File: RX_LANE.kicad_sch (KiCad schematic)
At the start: 1 part, among them U7 AD8285WBCPZ

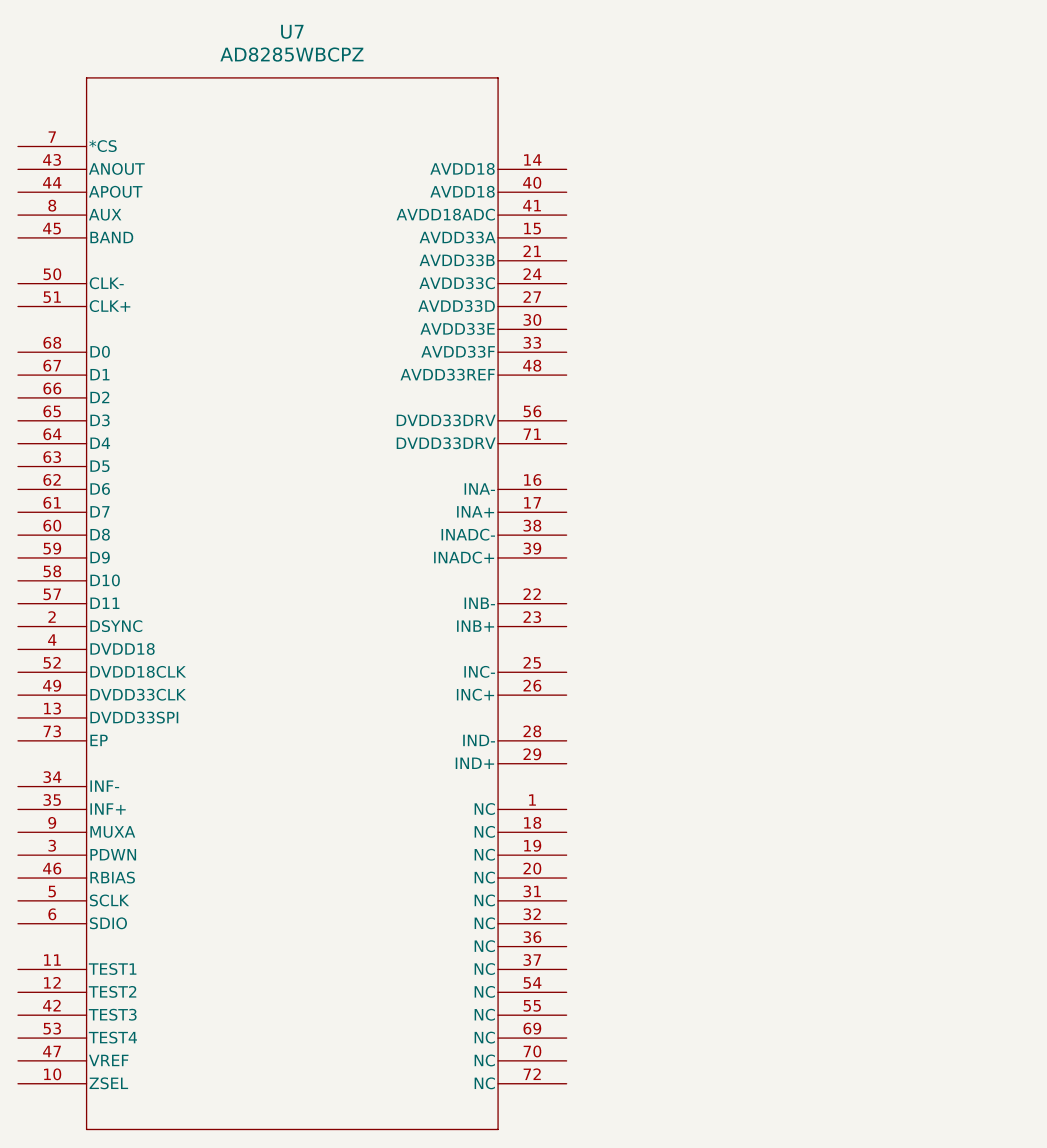
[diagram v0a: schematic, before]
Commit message: added ADC clock fanout, added 3A buck
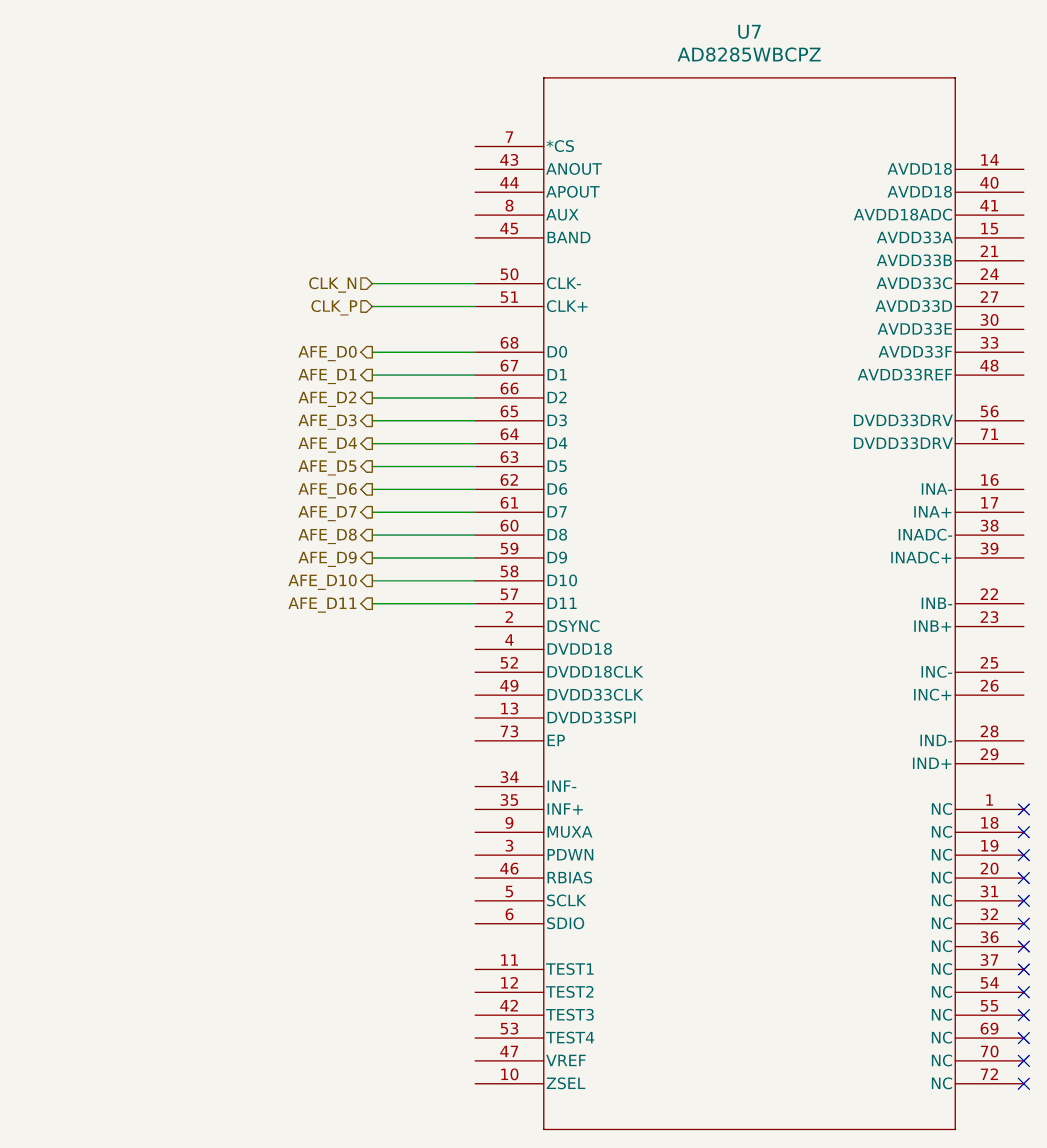
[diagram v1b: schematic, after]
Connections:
- net CLK_N: now reaches U7.50 (CLK-)
- net CLK_P: now reaches U7.51 (CLK+)
- net AFE_D11: now reaches U7.57 (D11)
- net AFE_D10: now reaches U7.58 (D10)
- net AFE_D9: now reaches U7.59 (D9)
- net AFE_D8: now reaches U7.60 (D8)
- net AFE_D7: now reaches U7.61 (D7)
- net AFE_D6: now reaches U7.62 (D6)
- net AFE_D5: now reaches U7.63 (D5)
- net AFE_D4: now reaches U7.64 (D4)
- net AFE_D3: now reaches U7.65 (D3)
- net AFE_D2: now reaches U7.66 (D2)
- net AFE_D1: now reaches U7.67 (D1)
- net AFE_D0: now reaches U7.68 (D0)
- no-connect marks 0 -> 13
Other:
- moved on the sheet: U7

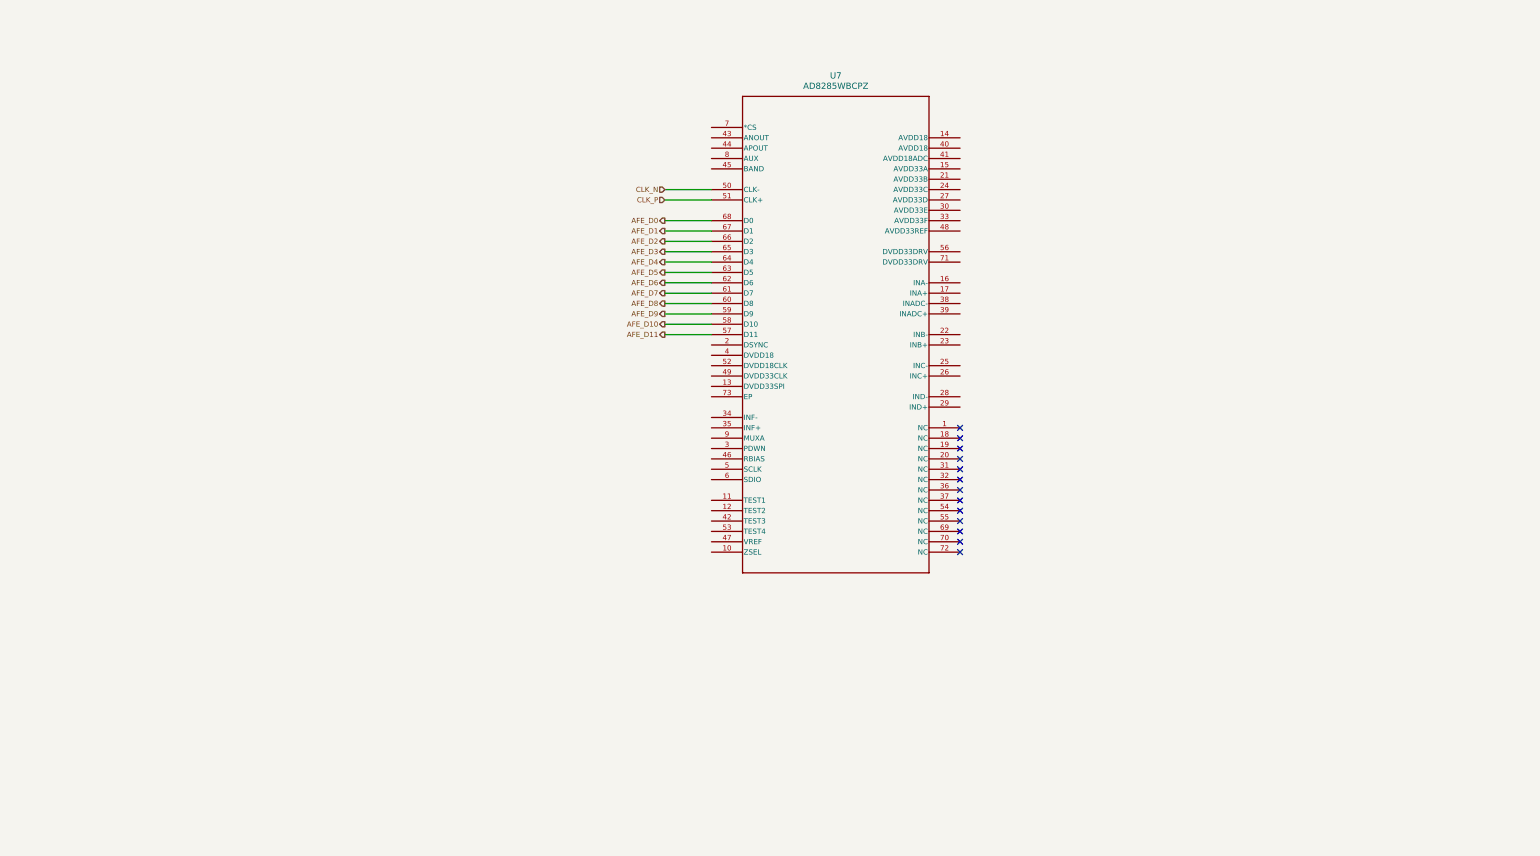
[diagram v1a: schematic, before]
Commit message: finished HV rails (revise, ai), added LDO instances, ready to bind & supply
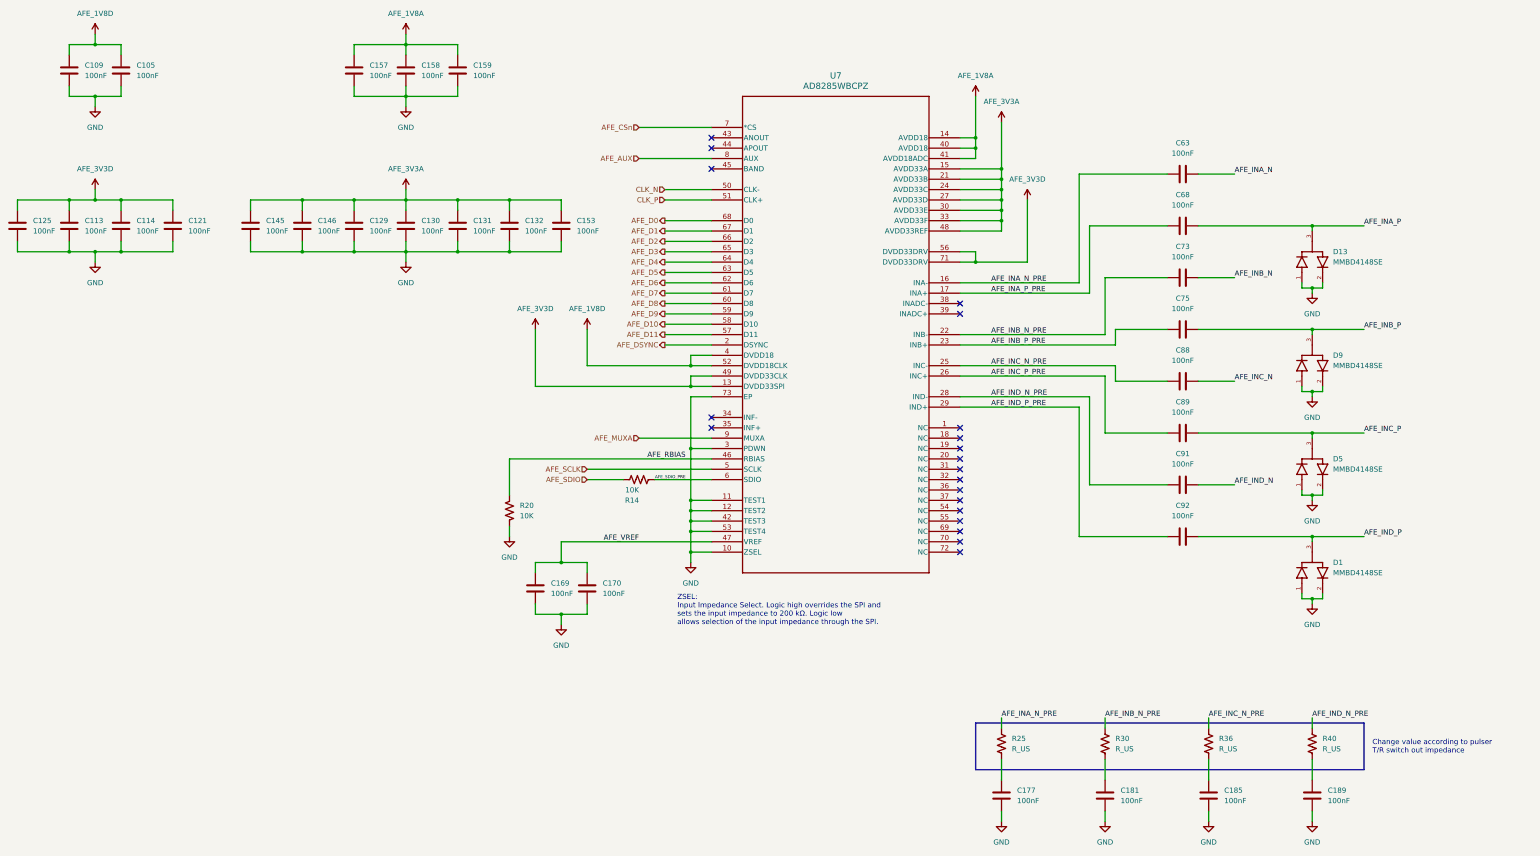
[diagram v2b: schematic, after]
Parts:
- added C105, C109, C113, C114, C121, C125, C129, C130, C131, C132, C145, C146, C153, C157, C158, C159, C169, C170, C177, C181, C185, C189, C63, C68, C73, C75, C88, C89, C91, C92: 100nF, symbol Device:C
- added D1, D13, D5, D9: MMBD4148SE, MMBD4148SE:SOT95P237X112-3N, symbol MMBD4148SE:MMBD4148SE
- added R14, R20: 10K, symbol Device:R_US
- added R25, R30, R36, R40: R_US, symbol Device:R_US
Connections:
- net GND: now reaches U7.10 (ZSEL)
- net GND: now also U7.11 (TEST1), U7.12 (TEST2), U7.3 (PDWN), U7.42 (TEST3), U7.53 (TEST4), U7.73 (EP), C105.2, C109.2, C113.2, C114.2, C121.2, C125.2, C129.2, C130.2, C131.2, C132.2, C145.2, C146.2, C153.2, C157.2, C158.2, C159.2, C169.2, C170.2, C177.2, C181.2, C185.2, C189.2, D1.1, D1.2, D13.1, D13.2, D5.1, D5.2, D9.1, D9.2, R20.2
- net AFE_3V3D: now reaches U7.13 (DVDD33SPI)
- net AFE_3V3D: now also U7.49 (DVDD33CLK), U7.56 (DVDD33DRV), U7.71 (DVDD33DRV), C113.1, C114.1, C121.1, C125.1
- net AFE_1V8A: now reaches U7.14 (AVDD18)
- net AFE_1V8A: now also U7.40 (AVDD18), U7.41 (AVDD18ADC), C157.1, C158.1, C159.1
- net AFE_3V3A: now reaches U7.15 (AVDD33A)
- net AFE_3V3A: now also U7.21 (AVDD33B), U7.24 (AVDD33C), U7.27 (AVDD33D), U7.30 (AVDD33E), U7.33 (AVDD33F), U7.48 (AVDD33REF), C129.1, C130.1, C131.1, C132.1, C145.1, C146.1, C153.1
- net AFE_INA_N_PRE: now reaches U7.16 (INA-)
- net AFE_INA_N_PRE: now also C63.2, R25.1
- net AFE_INA_P_PRE: now reaches U7.17 (INA+)
- net AFE_INA_P_PRE: now also C68.2
- net AFE_DSYNC: now reaches U7.2 (DSYNC)
- net AFE_INB_N_PRE: now reaches U7.22 (INB-)
- net AFE_INB_N_PRE: now also C73.2, R30.1
- net AFE_INB_P_PRE: now reaches U7.23 (INB+)
- net AFE_INB_P_PRE: now also C75.2
- net AFE_INC_N_PRE: now reaches U7.25 (INC-)
- net AFE_INC_N_PRE: now also C88.2, R36.1
- net AFE_INC_P_PRE: now reaches U7.26 (INC+)
- net AFE_INC_P_PRE: now also C89.2
- net AFE_IND_N_PRE: now reaches U7.28 (IND-)
- net AFE_IND_N_PRE: now also C91.2, R40.1
- net AFE_IND_P_PRE: now reaches U7.29 (IND+)
- net AFE_IND_P_PRE: now also C92.2
- net AFE_1V8D: now reaches U7.4 (DVDD18)
- net AFE_1V8D: now also U7.52 (DVDD18CLK), C105.1, C109.1
- net AFE_RBIAS: now reaches U7.46 (RBIAS)
- net AFE_RBIAS: now also R20.1
- net AFE_VREF: now reaches U7.47 (VREF)
- net AFE_VREF: now also C169.1, C170.1
- net AFE_SCLK: now reaches U7.5 (SCLK)
- net AFE_SDIO_PRE: now reaches U7.6 (SDIO)
- net AFE_SDIO_PRE: now also R14.2
- net AFE_CSn: now reaches U7.7 (*CS)
- net AFE_AUX: now reaches U7.8 (AUX)
- net AFE_MUXA: now reaches U7.9 (MUXA)
- new net: C177.1, R25.2
- new net: C189.1, R40.2
- new net: C181.1, R30.2
- new net: C185.1, R36.2
- new net AFE_INA_N: C63.1
- new net AFE_INA_P: C68.1, D13.3
- new net AFE_INB_N: C73.1
- new net AFE_INB_P: C75.1, D9.3
- new net AFE_INC_N: C88.1
- new net AFE_INC_P: C89.1, D5.3
- new net AFE_IND_N: C91.1
- new net AFE_IND_P: C92.1, D1.3
- new net AFE_SDIO: R14.1
- no-connect marks 13 -> 20
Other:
- note added: "Change value according to pulser T/R switch out impedance"
- note added: "ZSEL: Input Impedance Select. Logic high overrides the SPI and sets the input impedance to 200 kΩ. Logic low allows selection of the input impedance through the SPI."

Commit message: almost finished, phew! just dd +/- 5v rails, connect the SDIO & power enable pins and figure out the rest of the clocking chain
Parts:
- added R21, R28: 10K, symbol Device:R_US
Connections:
- net AFE_AUX: now also R21.1
- net AFE_MUXA: now also R28.1
- net GND: now also R21.2, R28.2
- net AFE_1V8A renamed 1V8A
- net AFE_1V8D renamed 1V8D
- net AFE_3V3A renamed 3V3A
- net AFE_3V3D renamed 3V3D
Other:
- moved on the sheet: C129, C130, C131, C132, C145, C146, C153, C157, C158, C159

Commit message: DONE! hust needs a final revision, checking termination throughout the circuit and verifying the signal chain
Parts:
- removed C63, C73, C88, C91: 100nF, symbol Device:C
- removed R36, R40: R_US, symbol Device:R_US
- added R38, R99: 8R, symbol Device:R_US
- R25, R30: value R_US -> 8R
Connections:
- net AFE_INC_N_PRE: now also R38.1
- net AFE_IND_N_PRE: now also R99.1
- net at C189.1: now also R99.2
- net at C185.1: now also R38.2

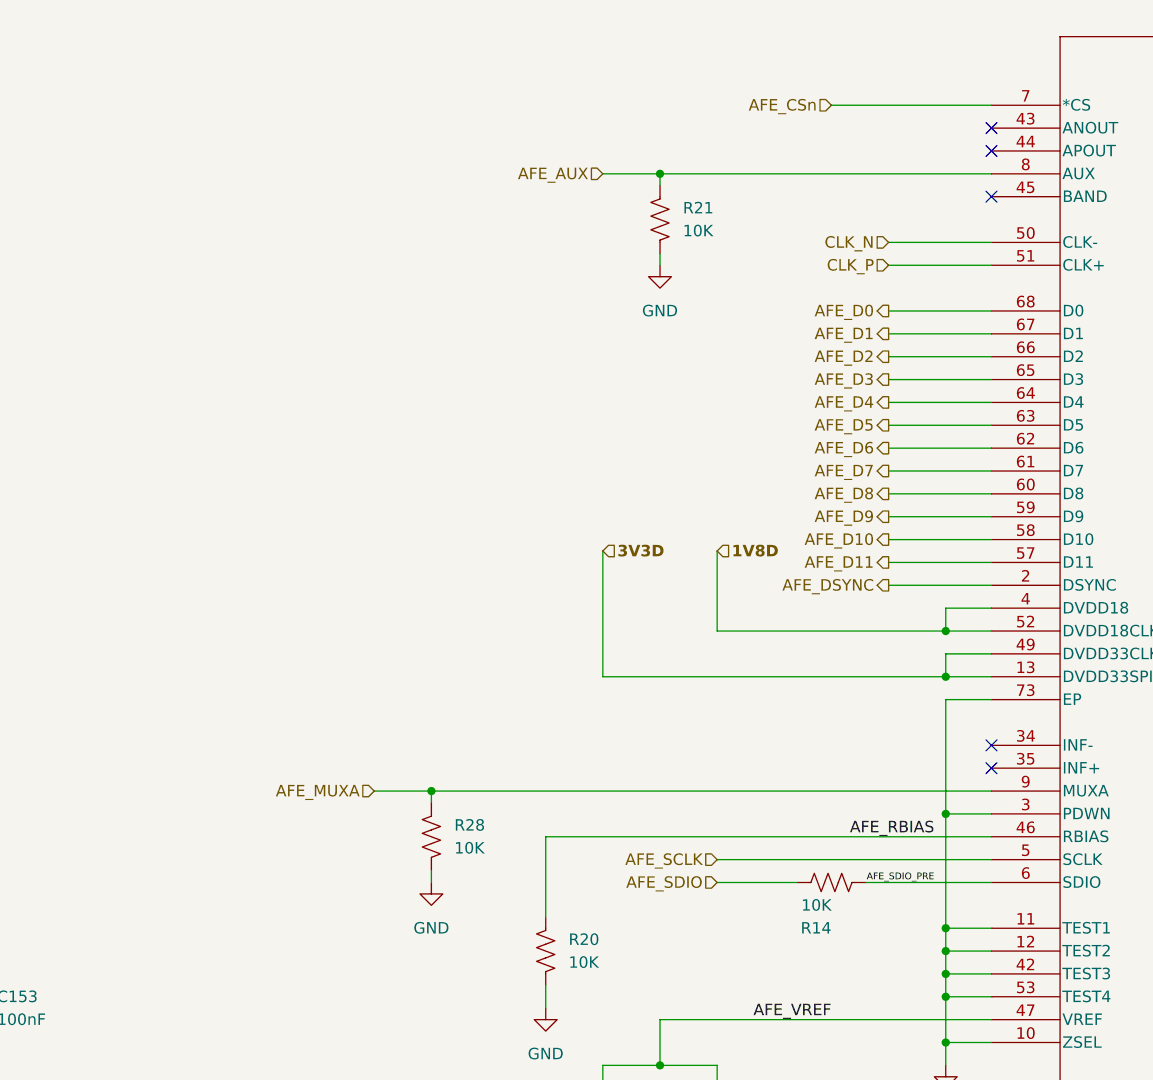
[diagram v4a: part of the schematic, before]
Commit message: HDMI was requested so add it and give the signal chain a final revision
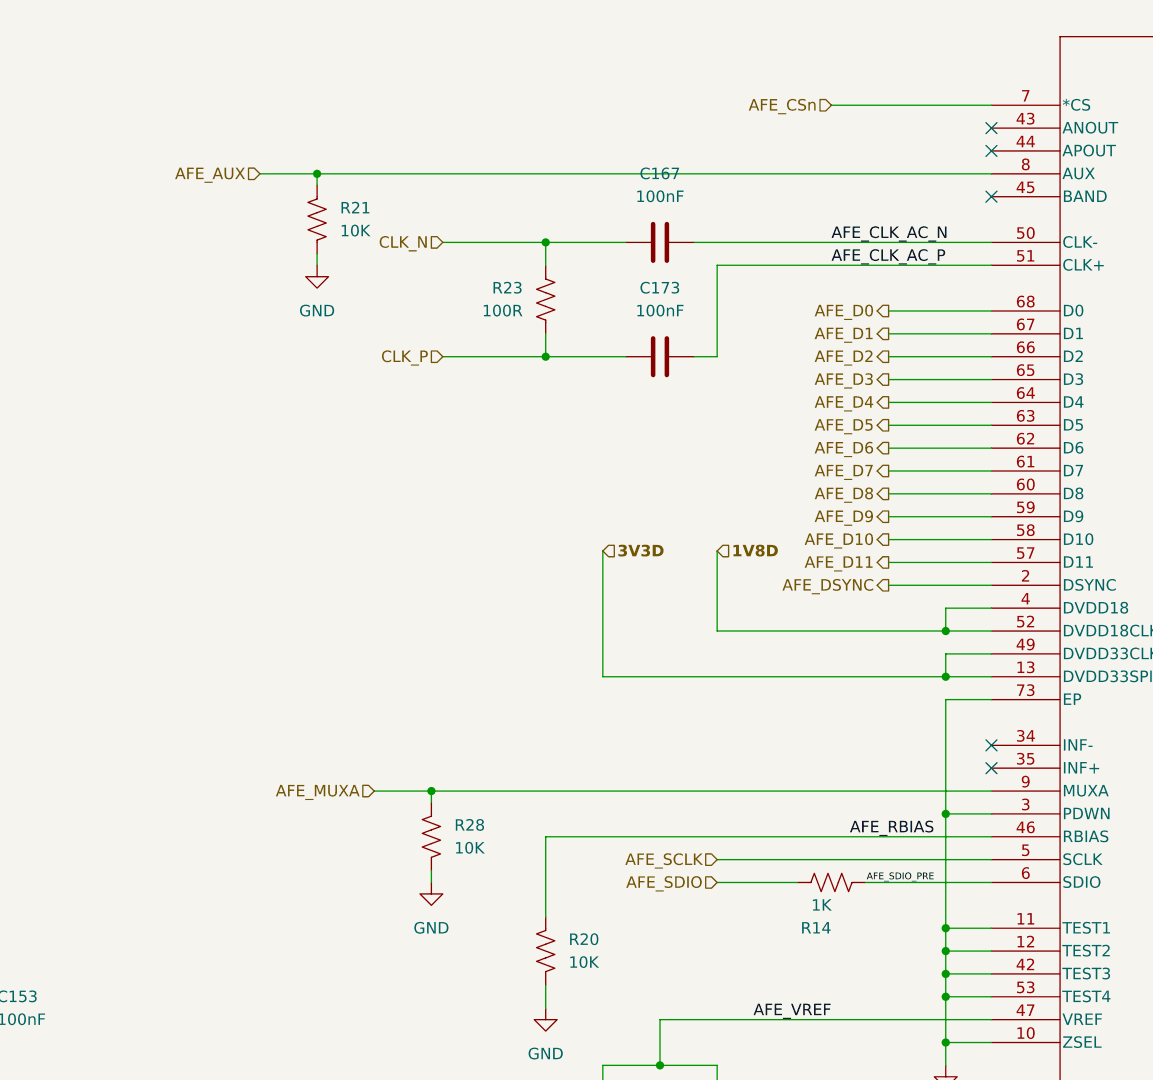
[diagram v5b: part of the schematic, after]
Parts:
- added C167, C173: 100nF, symbol Device:C
- added R23: 100R, symbol Device:R_US
- R14: value 10K -> 1K
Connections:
- net CLK_N: now also C167.1, R23.1; no longer U7.50 (CLK-)
- net CLK_P: now also C173.1, R23.2; no longer U7.51 (CLK+)
- new net AFE_CLK_AC_N: C167.2, U7.50 (CLK-)
- new net AFE_CLK_AC_P: C173.2, U7.51 (CLK+)
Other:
- moved on the sheet: R21

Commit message: ALL IS DONE EXCEPT HDMI PLEASE HELP
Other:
- note added: "Forces channel A to the ADC if AUX is not asserted."
- note added: "Forces the auxiliary channel (INADC) to the ADC."
- note added: "R_series recommended by datasheet"
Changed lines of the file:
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@@
+		)
+	)
+	(text "Forces channel A to the ADC\nif AUX is not asserted."
+		(exclude_from_sim no)
+		(at 104.14 119.888 0)
+		(effects
+			(font
+				(size 1.27 1.27)
+				(thickness 0.254)
+				(bold yes)
+			)
+			(justify left)
+		)
+	)
+	(text "R_series recommended\nby datasheet"
+		(exclude_from_sim no)
+		(at 174.752 140.462 0)
+		(effects
+			(font
+				(size 1.27 1.27)
+				(thickness 0.1588)
+			)
+			(justify left)
 		)
 	)
@@
 			)
 			(justify left)
+		)
+	)
+	(text "Forces the auxiliary channel (INADC)\nto the ADC."
+		(exclude_from_sim no)
+		(at 99.314 51.562 0)
+		(effects
+			(font
+				(size 1.27 1.27)
+				(thickness 0.254)
+				(bold yes)
+			)
+			(justify left)
